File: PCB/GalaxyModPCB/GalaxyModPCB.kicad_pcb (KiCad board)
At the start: 2 copper layers, 63.5 x 38.2 mm, 55 parts, among them J1 LED RGBW Connector, J2 USB to UART, J3 Motor Connector, J4 Projector Connector, J6 Power Header, J7 Boot mode, Q1 IRLML0030, Q2 IRLML0030, Q3 IRLML0030, Q4 IRLML0030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

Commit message: Fixed mounting holes
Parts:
- added H3: MountingHole, MountingHole:MountingHole_2.5mm, F.Cu at (170.0, 78.5)
- added H4: MountingHole, MountingHole:MountingHole_2.5mm, F.Cu at (170.0, 85.0)
- H1, H2: value MountingHole_Pad -> MountingHole; footprint MountingHole:MountingHole_2.2mm_M2_ISO7380_Pad -> MountingHole:MountingHole_2mm
- moved H1 11.0 mm to (181.6, 78.0)
- moved H2 11.0 mm to (176.1, 78.0)
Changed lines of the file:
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@@
     )
-  )
-  (footprint "MountingHole:MountingHole_2.2mm_M2_ISO7380_Pad" (layer "F.Cu")
-    (at 165.275 80.275)
-    (descr "Mounting Hole 2.2mm, M2, ISO7380")
-    (tags "mounting hole 2.2mm m2 iso7380")
-    (property "Sheetfile" "File: GalaxyModPCB.kicad_sch")
-    (property "Sheetname" "")
-    (attr exclude_from_pos_files)
-    (fp_text reference "H2" (at 0 -2.75) (layer "F.SilkS")
-      (effects (font (size 1 1) (thickness 0.15)))
-    )
-    (fp_text value "MountingHole_Pad" (at 0 2.75) (layer "F.Fab")
-      (effects (font (size 1 1) (thickness 0.15)))
-    )
-    (fp_text user "${REFERENCE}" (at 0 0) (layer "F.Fab")
-      (effects (font (size 1 1) (thickness 0.15)))
-    )
-    (fp_circle (center 0 0) (end 1.75 0) (layer "Cmts.User") (width 0.15) (fill none))
-    (fp_circle (center 0 0) (end 2 0) (layer "F.CrtYd") (width 0.05) (fill none))
-    (pad "1" thru_hole circle (at 0 0) (size 3.5 3.5) (drill 2.2) (layers *.Cu *.Mask)
-      (net 2 "GNDREF") (pinfunction "1") (pintype "input"))
   )
   (footprint "Resistor_SMD:R_0805_2012Metric_Pad1.20x1.40mm_HandSolder" (layer "F.Cu")
@@
     )
   )
-  (footprint "MountingHole:MountingHole_2.2mm_M2_ISO7380_Pad" (layer "F.Cu")
-    (at 170.825 80.275)
-    (descr "Mounting Hole 2.2mm, M2, ISO7380")
-    (tags "mounting hole 2.2mm m2 iso7380")
-    (property "Sheetfile" "File: GalaxyModPCB.kicad_sch")
-    (property "Sheetname" "")
-    (attr exclude_from_pos_files)
-    (fp_text reference "H1" (at 0 -2.75) (layer "F.SilkS")
-      (effects (font (size 1 1) (thickness 0.15)))
-    )
-    (fp_text value "MountingHole_Pad" (at 0 2.75) (layer "F.Fab")
-      (effects (font (size 1 1) (thickness 0.15)))
-    )
-    (fp_text user "${REFERENCE}" (at 0 0) (layer "F.Fab")
-      (effects (font (size 1 1) (thickness 0.15)))
-    )
-    (fp_circle (center 0 0) (end 1.75 0) (layer "Cmts.User") (width 0.15) (fill none))
-    (fp_circle (center 0 0) (end 2 0) (layer "F.CrtYd") (width 0.05) (fill none))
-    (pad "1" thru_hole circle (at 0 0) (size 3.5 3.5) (drill 2.2) (layers *.Cu *.Mask)
-      (net 2 "GNDREF") (pinfunction "1") (pintype "input"))
-  )
   (footprint "Resistor_SMD:R_0805_2012Metric_Pad1.20x1.40mm_HandSolder" (layer "F.Cu")
     (at 124 54 90)
@@
       (rotate (xyz 0 0 0))
     )
+  )
+  (footprint "MountingHole:MountingHole_2.5mm" (layer "F.Cu")
+    (at 170 78.45)
+    (descr "Mounting Hole 2.5mm, no annular")
+    (tags "mounting hole 2.5mm no annular")
+    (property "Sheetfile" "File: GalaxyModPCB.kicad_sch")
+    (property "Sheetname" "")
+    (attr exclude_from_pos_files)
+    (fp_text reference "H3" (at 0 -3.5) (layer "F.SilkS")
+      (effects (font (size 1 1) (thickness 0.15)))
+    )
+    (fp_text value "MountingHole" (at 0 3.5) (layer "F.Fab")
+      (effects (font (size 1 1) (thickness 0.15)))
+    )
+    (fp_text user "${REFERENCE}" (at 0 0) (layer "F.Fab")
+      (effects (font (size 1 1) (thickness 0.15)))
+    )
+    (fp_circle (center 0 0) (end 2.5 0) (layer "Cmts.User") (width 0.15) (fill none))
+    (fp_circle (center 0 0) (end 2.75 0) (layer "F.CrtYd") (width 0.05) (fill none))
+    (pad "" np_thru_hole circle (at 0 0) (size 2.5 2.5) (drill 2.5) (layers *.Cu *.Mask))
   )
   (footprint "Diode_SMD:D_0805_2012Metric_Pad1.15x1.40mm_HandSolder" (layer "F.Cu")
@@
     )
   )
+  (footprint "MountingHole:MountingHole_2mm" (layer "F.Cu")
+    (at 176.05 77.95)
+    (descr "Mounting Hole 2mm, no annular")
+    (tags "mounting hole 2mm no annular")
+    (property "Sheetfile" "File: GalaxyModPCB.kicad_sch")
+    (property "Sheetname" "")
+    (attr exclude_from_pos_files)
+    (fp_text reference "H2" (at 0 -3.2) (layer "F.SilkS")
+      (effects (font (size 1 1) (thickness 0.15)))
+    )
+    (fp_text value "MountingHole" (at 0 3.1) (layer "F.Fab")
+      (effects (font (size 1 1) (thickness 0.15)))
+    )
+    (fp_text user "${REFERENCE}" (at 0 0) (layer "F.Fab")
+      (effects (font (size 1 1) (thickness 0.15)))
+    )
+    (fp_circle (center 0 0) (end 2 0) (layer "Cmts.User") (width 0.15) (fill none))
+    (fp_circle (center 0 0) (end 2.25 0) (layer "F.CrtYd") (width 0.05) (fill none))
+    (pad "" np_thru_hole circle (at 0 0) (size 2 2) (drill 2) (layers *.Cu *.Mask))
+  )
   (footprint "Package_TO_SOT_SMD:SOT-23" (layer "F.Cu")
     (at 164 65 180)
@@
     )
   )
+  (footprint "MountingHole:MountingHole_2.5mm" (layer "F.Cu")
+    (at 170 85)
+    (descr "Mounting Hole 2.5mm, no annular")
+    (tags "mounting hole 2.5mm no annular")
+    (property "Sheetfile" "File: GalaxyModPCB.kicad_sch")
+    (property "Sheetname" "")
+    (attr exclude_from_pos_files)
+    (fp_text reference "H4" (at 0 -3.5) (layer "F.SilkS")
+      (effects (font (size 1 1) (thickness 0.15)))
+    )
+    (fp_text value "MountingHole" (at 0 3.5) (layer "F.Fab")
+      (effects (font (size 1 1) (thickness 0.15)))
+    )
+    (fp_text user "${REFERENCE}" (at 0 0) (layer "F.Fab")
+      (effects (font (size 1 1) (thickness 0.15)))
+    )
+    (fp_circle (center 0 0) (end 2.5 0) (layer "Cmts.User") (width 0.15) (fill none))
+    (fp_circle (center 0 0) (end 2.75 0) (layer "F.CrtYd") (width 0.05) (fill none))
+    (pad "" np_thru_hole circle (at 0 0) (size 2.5 2.5) (drill 2.5) (layers *.Cu *.Mask))
+  )
+  (footprint "MountingHole:MountingHole_2mm" (layer "F.Cu")
+    (at 181.6 77.95)
+    (descr "Mounting Hole 2mm, no annular")
+    (tags "mounting hole 2mm no annular")
+    (property "Sheetfile" "File: GalaxyModPCB.kicad_sch")
+    (property "Sheetname" "")
+    (attr exclude_from_pos_files)
+    (fp_text reference "H1" (at 0 -3.2) (layer "F.SilkS")
+      (effects (font (size 1 1) (thickness 0.15)))
+    )
+    (fp_text value "MountingHole" (at 0 3.1) (layer "F.Fab")
+      (effects (font (size 1 1) (thickness 0.15)))
+    )
+    (fp_text user "${REFERENCE}" (at 0 0) (layer "F.Fab")
+      (effects (font (size 1 1) (thickness 0.15)))
+    )
+    (fp_circle (center 0 0) (end 2 0) (layer "Cmts.User") (width 0.15) (fill none))
+    (fp_circle (center 0 0) (end 2.25 0) (layer "F.CrtYd") (width 0.05) (fill none))
+    (pad "" np_thru_hole circle (at 0 0) (size 2 2) (drill 2) (layers *.Cu *.Mask))
+  )
   (footprint "Resistor_SMD:R_0805_2012Metric_Pad1.20x1.40mm_HandSolder" (layer "F.Cu")

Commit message: Placed mounting holes
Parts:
- moved H1 61.4 mm to (124.5, 55.5)
- moved H3 49.1 mm to (124.5, 60.0)
- moved H2 28.2 mm to (159.0, 55.5)
- moved H4 27.3 mm to (159.0, 60.0)
- moved R38 1.58 mm to (124.5, 52.5), turned to 180 degrees
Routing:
- net Net-(C10-Pad1): track 79.0 -> 90.0 mm
- net Net-(C5-Pad1): track 27.6 -> 27.1 mm
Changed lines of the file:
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@@
   )
   (footprint "Resistor_SMD:R_0805_2012Metric_Pad1.20x1.40mm_HandSolder" (layer "F.Cu")
-    (at 124 54 90)
+    (at 124.5 52.5 180)
     (descr "Resistor SMD 0805 (2012 Metric), square (rectangular) end terminal, IPC_7351 nominal with elongated pad for handsoldering. (Body size source: IPC-SM-782 page 72, https://www.pcb-3d.com/wordpress/wp-content/uploads/ipc-sm-782a_amendment_1_and_2.pdf), generated with kicad-footprint-generator")
     (tags "resistor handsolder")
@@
     (property "Sheetname" "")
     (attr smd)
-    (fp_text reference "R38" (at 2 2 180) (layer "F.SilkS")
-      (effects (font (size 1 1) (thickness 0.15)))
-    )
-    (fp_text value "10K" (at 1 3 180) (layer "F.Fab")
-      (effects (font (size 1 1) (thickness 0.15)))
-    )
-    (fp_text user "${REFERENCE}" (at 0 0 90) (layer "F.Fab")
+    (fp_text reference "R38" (at -3.5 0 180) (layer "F.SilkS")
+      (effects (font (size 1 1) (thickness 0.15)))
+    )
+    (fp_text value "10K" (at -3.5 1.5 180) (layer "F.Fab")
+      (effects (font (size 1 1) (thickness 0.15)))
+    )
+    (fp_text user "${REFERENCE}" (at 0 0) (layer "F.Fab")
       (effects (font (size 0.5 0.5) (thickness 0.08)))
     )
@@
     (fp_line (start -1 -0.625) (end 1 -0.625) (layer "F.Fab") (width 0.1))
     (fp_line (start 1 0.625) (end -1 0.625) (layer "F.Fab") (width 0.1))
-    (pad "1" smd roundrect (at -1 0 90) (size 1.2 1.4) (layers "F.Cu" "F.Paste" "F.Mask") (roundrect_rratio 0.208333)
+    (pad "1" smd roundrect (at -1 0 180) (size 1.2 1.4) (layers "F.Cu" "F.Paste" "F.Mask") (roundrect_rratio 0.208333)
       (net 2 "GNDREF") (pintype "passive"))
-    (pad "2" smd roundrect (at 1 0 90) (size 1.2 1.4) (layers "F.Cu" "F.Paste" "F.Mask") (roundrect_rratio 0.208333)
+    (pad "2" smd roundrect (at 1 0 180) (size 1.2 1.4) (layers "F.Cu" "F.Paste" "F.Mask") (roundrect_rratio 0.208333)
       (net 3 "Net-(C5-Pad1)") (pintype "passive"))
     (model "${KICAD6_3DMODEL_DIR}/Resistor_SMD.3dshapes/R_0805_2012Metric.wrl"
@@
   )
   (footprint "MountingHole:MountingHole_2.5mm" (layer "F.Cu")
-    (at 170 78.45)
+    (at 124.5 60)
     (descr "Mounting Hole 2.5mm, no annular")
     (tags "mounting hole 2.5mm no annular")
@@
     (property "Sheetname" "")
     (attr exclude_from_pos_files)
-    (fp_text reference "H3" (at 0 -3.5) (layer "F.SilkS")
+    (fp_text reference "H3" (at -2.5 0) (layer "F.SilkS")
       (effects (font (size 1 1) (thickness 0.15)))
     )
@@
     (property "Sheetname" "")
     (attr smd)
-    (fp_text reference "SW4" (at 0 -4.05) (layer "F.SilkS")
+    (fp_text reference "SW4" (at 0 -2) (layer "F.SilkS")
       (effects (font (size 1 1) (thickness 0.15)))
     )
@@
   )
   (footprint "MountingHole:MountingHole_2mm" (layer "F.Cu")
-    (at 176.05 77.95)
+    (at 159 55.5)
     (descr "Mounting Hole 2mm, no annular")
     (tags "mounting hole 2mm no annular")
@@
     (property "Sheetname" "")
     (attr smd)
-    (fp_text reference "SW1" (at 0 -4.05) (layer "F.SilkS")
+    (fp_text reference "SW1" (at 0 -2) (layer "F.SilkS")
       (effects (font (size 1 1) (thickness 0.15)))
     )
@@
   )
   (footprint "MountingHole:MountingHole_2.5mm" (layer "F.Cu")
-    (at 170 85)
+    (at 159 60)
     (descr "Mounting Hole 2.5mm, no annular")
     (tags "mounting hole 2.5mm no annular")
@@
   )
   (footprint "MountingHole:MountingHole_2mm" (layer "F.Cu")
-    (at 181.6 77.95)
+    (at 124.5 55.5)
     (descr "Mounting Hole 2mm, no annular")
     (tags "mounting hole 2mm no annular")
@@
     (property "Sheetname" "")
     (attr exclude_from_pos_files)
-    (fp_text reference "H1" (at 0 -3.2) (layer "F.SilkS")
+    (fp_text reference "H1" (at -2 0) (layer "F.SilkS")
       (effects (font (size 1 1) (thickness 0.15)))
     )
@@
     )
   )
+  (gr_line (start 179.5 55.5) (end 179.5 60) (layer "B.Cu") (width 0.2))
+  (gr_line (start 173.5 47.5) (end 159 47.5) (layer "B.Cu") (width 0.2))
+  (gr_line (start 177 51) (end 177 55.5) (layer "B.Cu") (width 0.2))
   (gr_arc (start 147 51) (mid 142 56) (end 137 51) (layer "Edge.Cuts") (width 0.1))
   (gr_line (start 143 89.16) (end 159.53 89.16) (layer "Edge.Cuts") (width 0.1))
@@
   (segment (start 113 52.775) (end 113.025 52.75) (width 0.5) (layer "F.Cu") (net 3))
   (segment (start 119.75 53.975) (end 119.75 64.75) (width 0.5) (layer "F.Cu") (net 3))
-  (segment (start 120.975 52.75) (end 123.75 52.75) (width 0.5) (layer "F.Cu") (net 3))
-  (segment (start 123.75 52.75) (end 124 53) (width 0.5) (layer "F.Cu") (net 3))
+  (segment (start 120.975 52.75) (end 123.25 52.75) (width 0.5) (layer "F.Cu") (net 3))
+  (segment (start 123.25 52.75) (end 123.5 52.5) (width 0.5) (layer "F.Cu") (net 3))
   (via (at 126 71) (size 0.8) (drill 0.4) (layers "F.Cu" "B.Cu") (net 3))
   (segment (start 124.34 71) (end 124.25 71.09) (width 0.5) (layer "B.Cu") (net 3))
@@
   (segment (start 127.220046 67.28) (end 124.25 67.28) (width 0.5) (layer "B.Cu") (net 6))
   (segment (start 126 80) (end 126.05 79.95) (width 0.5) (layer "F.Cu") (net 7))
-  (segment (start 126.975 63.25) (end 120.975 57.25) (width 0.5) (layer "F.Cu") (net 7))
   (segment (start 142.9 77.15) (end 128.085051 77.15) (width 0.5) (layer "F.Cu") (net 7))
   (segment (start 154 61.95) (end 154 63.225) (width 0.5) (layer "F.Cu") (net 7))
   (segment (start 126.05 79.185051) (end 126.05 81) (width 0.5) (layer "F.Cu") (net 7))
   (segment (start 163.025 57.25) (end 157.025 63.25) (width 0.5) (layer "F.Cu") (net 7))
+  (segment (start 136.975 63.25) (end 138.225 62) (width 0.25) (layer "F.Cu") (net 7))
   (segment (start 157.025 63.25) (end 153.975 63.25) (width 0.5) (layer "F.Cu") (net 7))
   (segment (start 113 55.95) (end 113 57.225) (width 0.5) (layer "F.Cu") (net 7))
@@
   (segment (start 171 57.225) (end 170.975 57.25) (width 0.5) (layer "F.Cu") (net 7))
   (segment (start 151.05 69) (end 142.9 77.15) (width 0.5) (layer "F.Cu") (net 7))
+  (segment (start 120.975 58.949876) (end 120.975 57.25) (width 0.5) (layer "F.Cu") (net 7))
   (segment (start 128 76) (end 128 77.064949) (width 0.5) (layer "F.Cu") (net 7))
   (segment (start 129 61.95) (end 129 63.225) (width 0.5) (layer "F.Cu") (net 7))
+  (segment (start 125.275124 63.25) (end 120.975 58.949876) (width 0.5) (layer "F.Cu") (net 7))
+  (segment (start 138.225 62) (end 144.775 62) (width 0.25) (layer "F.Cu") (net 7))
+  (segment (start 129.025 63.25) (end 125.275124 63.25) (width 0.5) (layer "F.Cu") (net 7))
+  (segment (start 144.775 62) (end 146.025 63.25) (width 0.25) (layer "F.Cu") (net 7))
   (segment (start 154 63.225) (end 153.975 63.25) (width 0.5) (layer "F.Cu") (net 7))
-  (segment (start 129.025 63.25) (end 126.975 63.25) (width 0.5) (layer "F.Cu") (net 7))
   (segment (start 126.05 79.95) (end 126.05 81) (width 0.5) (layer "F.Cu") (net 7))
   (via (at 123 80) (size 0.8) (drill 0.4) (layers "F.Cu" "B.Cu") (net 7))

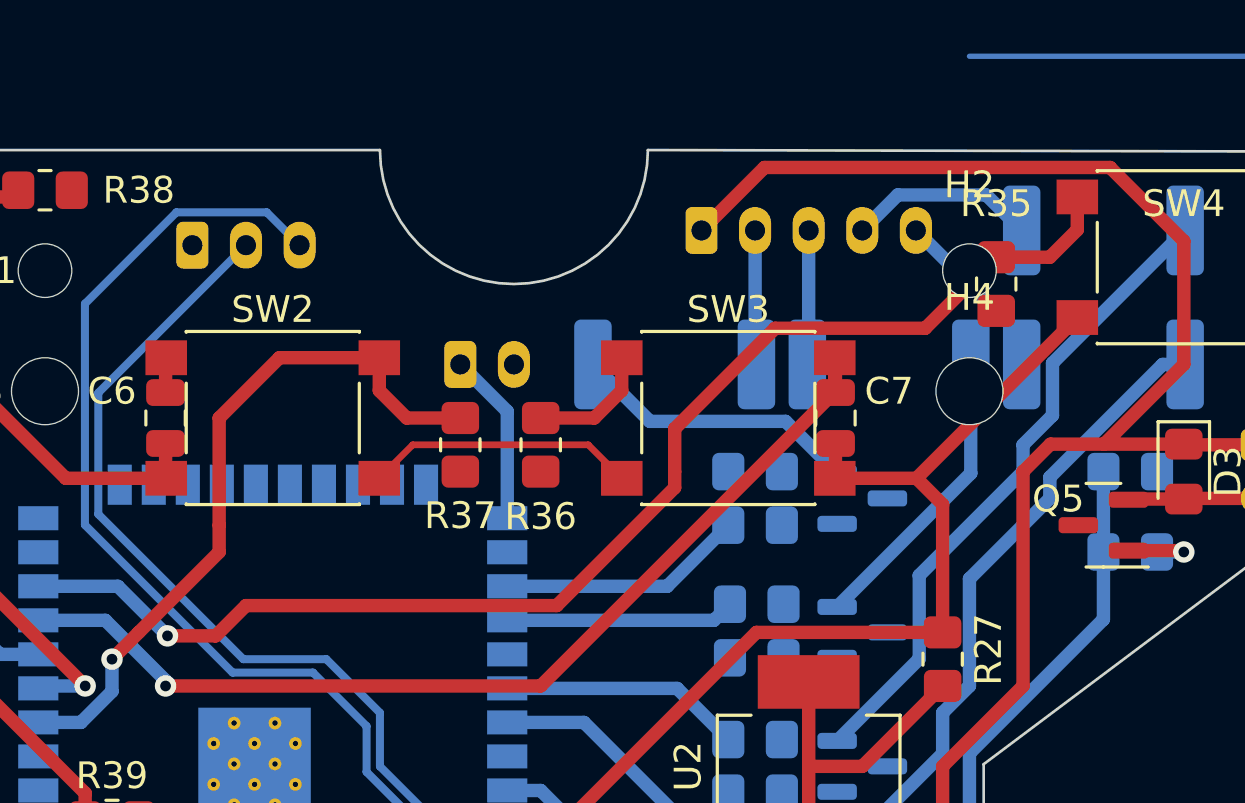
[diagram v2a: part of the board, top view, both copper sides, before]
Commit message: Accounted for mounting holes
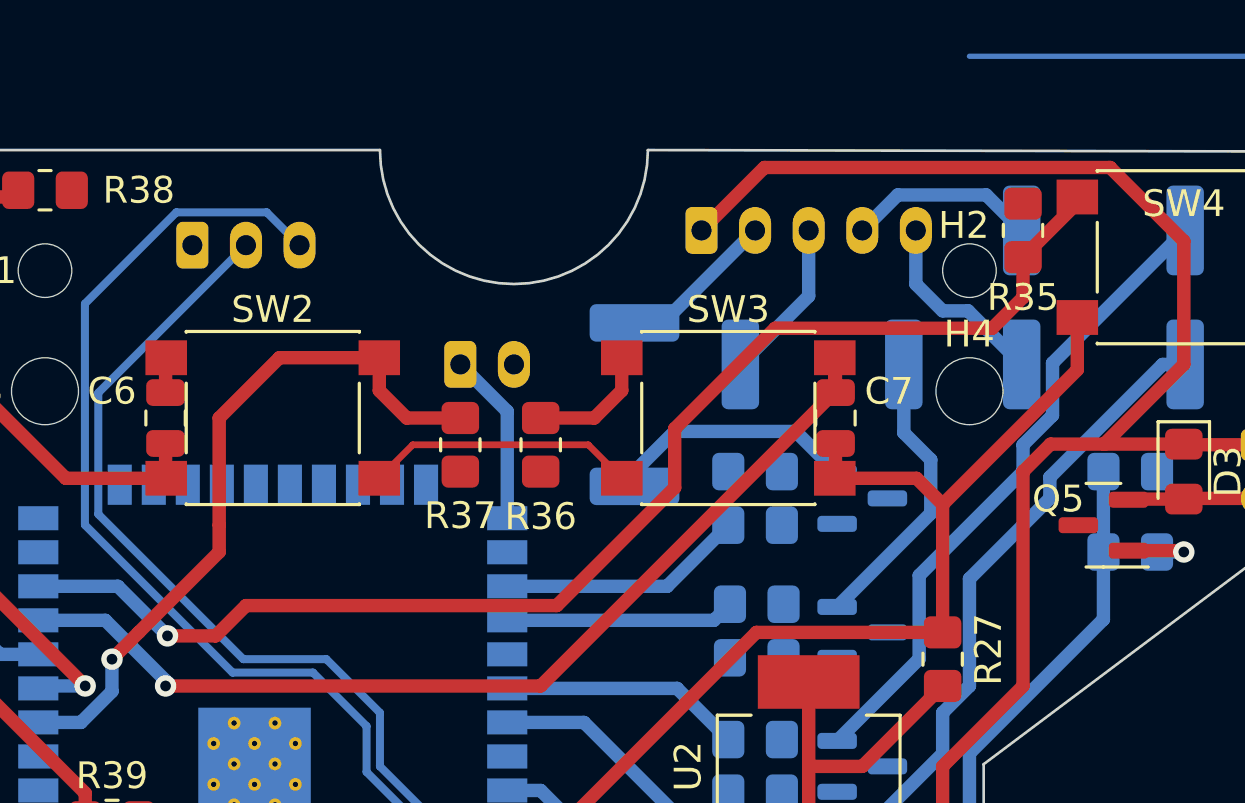
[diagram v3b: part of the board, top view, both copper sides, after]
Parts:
- moved R5 2.50 mm to (153.5, 59.0)
- moved R35 2.24 mm to (161.0, 54.0), turned to -90 degrees
- moved R1 2.12 mm to (146.5, 60.5), turned to -90 degrees
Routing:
- net Net-(J1-Pad5): track 6.64 -> 8.24 mm
- net Net-(Q1-Pad2): track 10.8 -> 9.38 mm
- net Net-(J1-Pad3): track 5.02 -> 6.06 mm
- net Net-(J1-Pad2): track 5.02 -> 5.93 mm
- net Net-(C10-Pad1): track 90.0 -> 90.6 mm
